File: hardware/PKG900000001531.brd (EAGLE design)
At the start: 80 x 50 mm, 297 parts, among them IC1 CAT24C256YI-G, IC2 FT232RQ, IC3 TPS62111, IC5 FT232RQ, IC6 SN74LVC1G126DCKR, IC7 SN74LVC1G126DCKR, J1 JST-GH-5H, J10 FPC-15VERT, J11 FPC-15VERT, J12 JST-GH-6H, J13 JST-GH-6H, J14 JST-GH-4H, J2 DF40HC(3.0)-100DS-0.4V(51), J3 USD_WURTH, J4 DIP-1, J5 SM10B-SRSS-TB, J7 USB-TYPE-C, J8 DF40HC(3.0)-100DS-0.4V(51), J9 CON8X3STD, Q1 FDN360P, Q2 DNP, Q3 FDN360P, Q4 FDN360P, Q6 FDN360P, U1 TPS2041BDGN, U10 DNP, U100 STM32H753II, U101 MIC94081, U102 USB2513, U105 TPS2121, U106 FM25V02A-DG, U107 TPD4E02B0410-USON, U108 BMP388, U109 MIC94081, U11 ICM-20602, U110 TCR2EF18, U13 USB3300-EZK-TR, U15 BMI088, U16 MIC94081, U17 TPD4E02B0410-USON, U18 TPD4E02B0410-USON, U2 TJA1051TK/3, U25 TPS2041BDGN, U26 TS3USB30, U3 TPD4E02B0410-USON, U4 EVQ, U5 G313-06329-00, U6 NCP308, U7 ICM-42605, U8 TPD4E02B0410-USON, U9 BMM150, Y1 24.000MHz, Y2 16.000MHz, Y3 32.768KHz CL6, Y4 24.000MHz

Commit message: Update hardware files for revision 2.
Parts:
- removed U$57: DNP, qualified_1:GEPPETTO_HOLE_2.9
- added R13, R47, R55, R56: 10K 1%, qualified_1:0201
- added R46: DNP, qualified_1:0201
- added R52, R54: 0R, qualified_1:0201
- added U30: TS3A5223, qualified_1:UQFN-10
- R77: value DNP -> 10K 1%
- moved C68 3.06 mm to (36.1, 10.5), turned to 270 degrees
- renumbered U4 to S3
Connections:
- removed net 3V3_SPEKTRUM$1: U16.1_1, U16.1_2
- removed net 5.USB_DEVICE_VBUS: FB4.1
- removed net 6.USB_DEVICE_VBUS: FB1.1
- new net 3V3_SPEKTRUM: J1.P4, U16.1_1, U16.1_2
- new net BMM150_PS: R46.2, R47.1, U9.A1
- new net UART_MUX_SEL$: R55.1, R56.2, U30.4, U30.8
- new net USART3_RX_DEBUG_FTDI: IC6.4, U30.2
- new net USART3_RX_DEBUG_JST: D5.A, U30.5
- new net USART3_TX_DEBUG_FTDI: IC5.2, U30.10
- new net USART3_TX_DEBUG_JST: J5.2, U3.1, U3.10, U30.7
- net 2.3.3V_VCC_3.3: now also U30.1; no longer J1.P4
- net 3V3_SENSORS: now also R47.2
- net 7.UART4_4W_RXD: now also R54.1
- net 7.UART4_4W_TXD: now also R52.1
- net BTN_A$22: now also S1.B@1
- net GND: now also R13.1, R46.1, R56.1, S1.A@2, U30.6; no longer U9.A1
- net SDO$1: now also R13.2
- net UART5_CTS_TELEM2: now also R1.2, R2.2
- net UART5_RTS_TELEM2: now also R3.2, R4.2
- net UART5_RX_TELEM2: now also R52.2
- net UART5_TX_TELEM2: now also R54.2
- net UART7_CTS_TELEM1: no longer R1.2, R2.2
- net UART7_RTS_TELEM1: no longer R3.2, R4.2
- net USART3_RX_DEBUG: now also U30.3; no longer D5.A, IC6.4
- net USART3_TX_DEBUG: now also U30.9; no longer IC5.2, J5.2, U3.1, U3.10
- net VBUS_SENSE: now also FB1.1, FB4.1, R55.2
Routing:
- net USART3_TX_DEBUG_JST: track 0.00 -> 84.3 mm, vias 0 -> 4
- net USART3_RX_DEBUG_JST: track 0.00 -> 64.5 mm, vias 0 -> 2
- net 3V3_SPEKTRUM: track 0.00 -> 59.9 mm, vias 0 -> 1
- net USART3_TX_DEBUG: track 93.0 -> 44.8 mm, vias 4 -> 2
- net UART5_CTS_TELEM2: track 0.00 -> 44.4 mm, vias 0 -> 3
- net UART5_RTS_TELEM2: track 0.00 -> 41.6 mm, vias 0 -> 3
- net 7.UART4_4W_RXD: track 0.00 -> 39.6 mm, vias 0 -> 3
- net 7.UART4_4W_TXD: track 0.00 -> 37.8 mm, vias 0 -> 3
- net VBUS_SENSE: track 43.0 -> 66.7 mm
- net USART3_RX_DEBUG: track 105.8 -> 84.9 mm, vias 3 -> 2
- net UART7_RTS_TELEM1: track 20.9 -> 0.00 mm, vias 2 -> 0
- net USART3_TX_DEBUG_FTDI: track 0.00 -> 16.8 mm
- net USART3_RX_DEBUG_FTDI: track 0.00 -> 12.6 mm, vias 0 -> 1
- net UART7_CTS_TELEM1: track 12.4 -> 0.00 mm, vias 2 -> 0
- net UART5_TX_TELEM2: track 0.00 -> 10.4 mm, vias 0 -> 1
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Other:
- board text added: "DFU"
- board text added: "OTG HS"

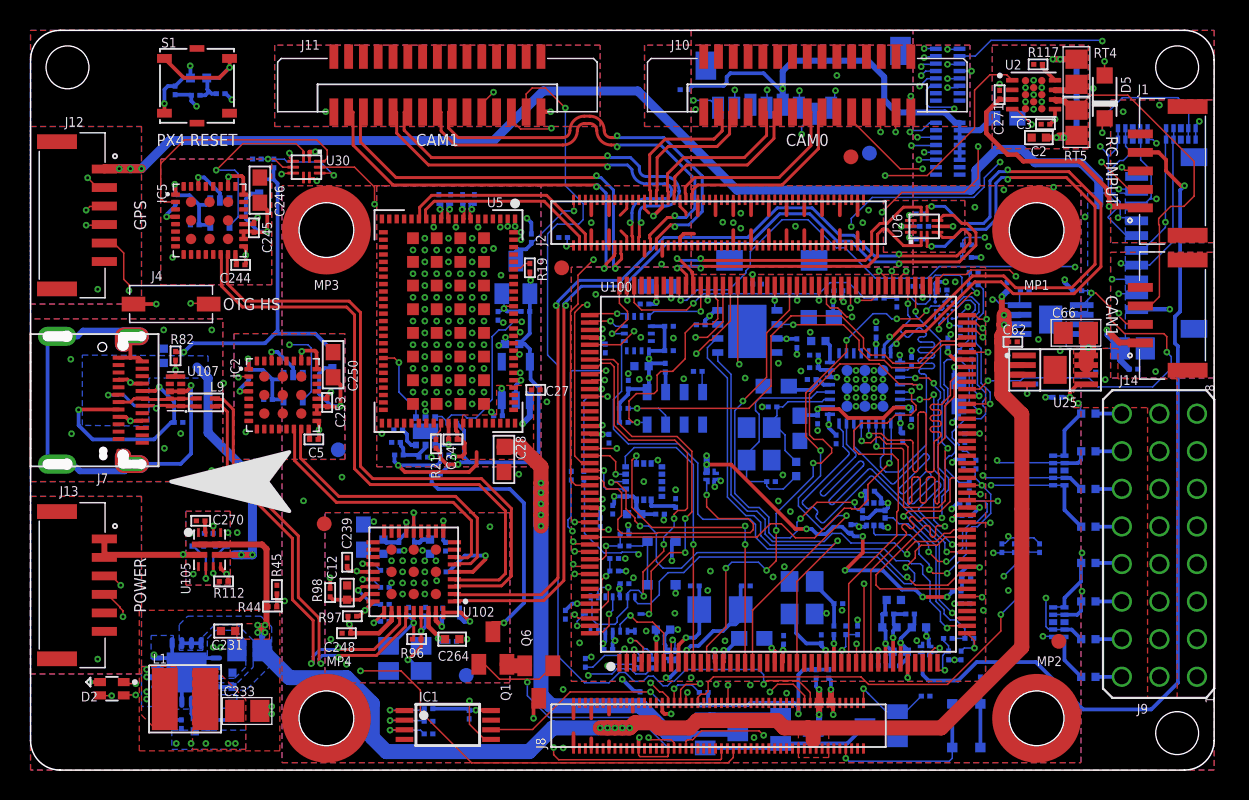
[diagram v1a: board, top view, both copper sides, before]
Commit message: Update board design files to v4.
Add ROS2 and Coral support information to the firmware docs.
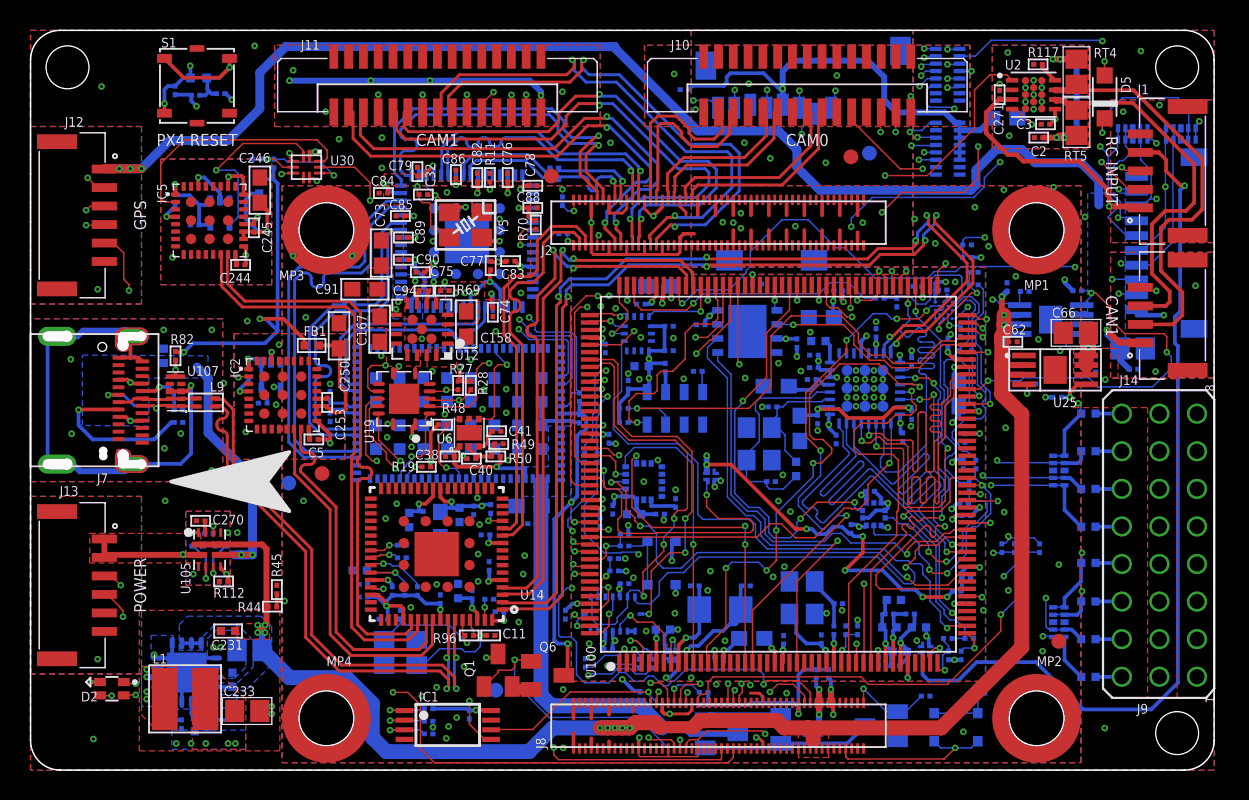
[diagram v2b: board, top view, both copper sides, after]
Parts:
- removed C103: 0.1uF, qualified_1@eagle_src_repo_a6c39d613d14f2251c563284af21e76ddd4db3e9:0201
- removed C242, C272, C273: 0.1uF, qualified_1:0201
- removed C264: 1.0uF, qualified_1:0402
- removed J4: DIP-1, qualified_1:CHS-01TA
- removed Q2: DNP, qualified_1:SOT23
- removed R116: DNP, qualified_1:0201
- removed R118, R121, R122: 0R, qualified_1:0201
- removed U102: USB2513, qualified_1:QFN36-6X6MM
- removed U110: TCR2EF18, qualified_1:SOT-23-5
- removed U26: TS3USB30, qualified_1:UQFN-10
- added C158, C167: 10uF, qualified_1:0603
- added C31, C96: 1.0uF, qualified_1:0402
- added C32: 10pF, qualified_1:0201
- added C72, C73, C74, C75, C76, C77, C78, C79, C82, C83, C84, C85, C86, C88, C89, C92, C93, C95, C97: 0.1uF, qualified_1:0201
- added C90, C91: 4.7uF / 16V, qualified_1:0603
- added C94: 6.8nF, qualified_1:0201
- added R58: 0R, qualified_1:0201
- added R68: 5K1, qualified_1:0201
- added R69, R70: 10K 1%, qualified_1:0201
- added U12: ADP1740ACPZ-1.2-R7, qualified_1:LFCSPWQ16
- added U14: USB2517-JZX, qualified_1:QFN64-9X9MM-FT2232HQ
- added U19: (no value), qualified_1:S-PVQFN-N14
- added U4: ASM1142, qualified_1:QFN64-9X9MM-FT2232HQ
- added Y5: 20.000MHz, qualified_1:CRYSTAL-3225
- C13, C16: value 1.0uF -> 0.1uF; device qualified_1:0402 -> qualified_1:0201
- C2: value DNP -> 4.7nF; device qualified_1:0402 -> qualified_1:0201
- R11: value 10K 1% -> 12K1
- R117: value DNP -> 10K 1%
- R20: value DNP -> 1K5
- R27, R28: value 10K 1% -> 1K5; device qualified_1@eagle_src_repo_a6c39d613d14f2251c563284af21e76ddd4db3e9:0201 -> qualified_1:0201
- R43, R9: value DNP -> 0R
- R5: value 0R -> 100K 1%
- RT4, RT5: value DNP -> 60R4
- U$2: device qualified_1:GEPPETTO_LABEL_SMALL -> qualified_1:UPVERTER_LABEL_SMALL
- U6: value NCP308 -> (none)
- moved R11 47.5 mm to (31.1, 40.0), flipped to the top
- moved R20 41.4 mm to (64.5, 5.50), turned to 270 degrees
- moved R27 32.8 mm to (28.9, 26.0), flipped to the top, turned to 90 degrees
- moved R28 32.5 mm to (29.8, 26.0), flipped to the top, turned to 90 degrees
- moved R5 21.0 mm to (31.1, 17.6)
- moved R19 15.2 mm to (26.8, 20.5), turned to 0 degrees
- moved C16 11.4 mm to (21.6, 31.6), turned to 180 degrees
- moved R21 10.2 mm to (37.1, 25.2), flipped to the bottom
- moved C27 9.05 mm to (33.9, 16.6), flipped to the bottom
- moved C34 8.66 mm to (37.1, 23.8), flipped to the bottom, turned to 270 degrees
- moved R43 8.12 mm to (20.2, 23.9), turned to 90 degrees
- moved R49 6.95 mm to (31.6, 22.1), flipped to the top
- moved C41 6.65 mm to (31.5, 22.9), flipped to the top
- moved R50 6.55 mm to (31.4, 21.2), flipped to the top
- moved U5 6.29 mm to (28.9, 24.1), flipped to the bottom, turned to 180 degrees
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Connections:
- removed net !PCIE_CLKREQ$17: Q2.2, R116.2, R20.2, U5.78
- removed net 1.USB_HS_VBUS: U13.4
- removed net 1.USB_MUX_D_N: U102.1, U26.5
- removed net 1.USB_MUX_D_P: U102.2, U26.3
- removed net 7.PCIE_CLK_N: R121.2, U5.10
- removed net 7.PCIE_CLK_P: R118.2, U5.11
- removed net CC$3: J7.A5, J7.B5, R89.2
- removed net INTR$17: U5.77
- removed net PCIE_TX_N$17: U5.4
- removed net PCIE_TX_P$17: U5.5
- removed net RPIBOOT_SWITCH$7: R11.2, S2.1, S2.2
- removed net SELECT: J4.2, R27.2, U26.10
- removed net USBMUX_OE$13: R28.2, U26.8
- removed net USB_CRFILT$4: C13.1, C272.1, U102.14
- removed net USB_PLLFILT$4: C242.1, C264.1, U102.34
- removed net USB_VBUS_DET$4: R97.2, U102.27
- removed net V1.8$17: C16.1, Q2.1, R116.1, R19.2, R21.2, R43.2, R48.2, U110.5
- new net !INT: U4.2
- new net !PCIE_WAKE: U4.25
- new net !RST$: R70.1, U4.9
- new net !SPI_CS$: U4.7
- new net !USB1_NOC: U4.28
- new net !USB2_NOC: U4.29
- new net 7.GPIO2_GPIO: J8.58, U19.11
- new net 7.GPIO3_GPIO: J8.56, U19.10
- new net 7.GPIO6_GPIO: J8.30, U19.12
- new net 7.GPIO7_GPIO: J8.37, U19.13
- new net 7.PCIE_NRESET: J2.9, R69.1, U4.30
- new net CC1$3: J7.A5, R68.2
- new net CC2$3: J7.B5, R89.2
- new net CFG_SEL2$: R5.2, U14.13
- new net I2C_SCL: R27.1, U19.5, U5.50
- new net I2C_SDA: R28.1, U19.4, U5.49
- new net PCIE_CLK_N: J2.12, U4.49
- new net PCIE_CLK_P: J2.10, U4.48
- new net PCIE_RX0__N: C93.2, U4.57
- new net PCIE_RX0__P: C92.2, U4.56
- new net PCIE_TX_N: J2.24, U4.53
- new net PCIE_TX_P: J2.22, U4.54
- new net PHY_PRG: U19.2, U5.84
- new net REXT$: R11.2, U4.59
- new net RPIBOOT_SWITCH$19: R20.2, S2.1, S2.2
- new net SPI_CLK$: U4.5
- new net SPI_DI$: U4.8
- new net SPI_DO$: U4.6
- new net UART_RX$: U4.10
- new net UART_TX$: U4.11
- new net USB1_N: U4.22, U5.14
- new net USB1_P: U4.23, U5.13
- new net USB1_PWREN: U4.26
- new net USB1_SSRX_N: U4.46, U5.4
- new net USB1_SSRX_P: U4.45, U5.5
- new net USB1_SSTX_N: C16.2, U4.43
- new net USB1_SSTX_P: C72.2, U4.42
- new net USB1_SSTX__N: C16.1, U5.7
- new net USB1_SSTX__P: C72.1, U5.8
- new net USB2_N: U4.18
- new net USB2_P: U4.19
- new net USB2_PWREN: U4.27
- new net USB2_SSRX_N: U4.37
- new net USB2_SSRX_P: U4.36
- new net USB2_SSTX_N: U4.40
- new net USB2_SSTX_P: U4.39
- new net USB_CRFILT$: C31.1, C95.1, U14.25
- new net USB_PLLFILT$: C96.1, C97.1, U14.62
- new net V1.2$: C167.1, C74.1, C75.1, C78.1, C79.1, C82.1, C83.1, C84.1, C89.1, C90.1, C91.1, U12.10, U12.11, U12.12, U12.13, U12.14, U12.9, U4.1, U4.12, U4.21, U4.33, U4.34, U4.35, U4.41, U4.47, U4.52, U4.58
- new net VBUS_DET$: R97.2, U14.44
- new net VCC1V1_SS$: C94.1, U12.7
- new net XI$: C32.2, U4.51, Y5.1
- new net XO$: C32.1, U4.50, Y5.3
- new net _PCIE_CLK_N: R43.2, U5.10
- new net _PCIE_CLK_P: R58.2, U5.11
- net 1.USB_HS_D_N: now also U14.1; no longer U26.6
- net 1.USB_HS_D_P: now also U14.2; no longer U26.2
- net 2.3.3V_VCC_3.3: now also C13.1, C158.1, C73.1, C76.1, C77.1, C85.1, C86.1, C88.1, R5.1, R69.2, R70.2, R91.1, U12.1, U12.15, U12.16, U12.2, U12.3, U12.4, U14.10, U14.24, U14.46, U14.5, U14.52, U14.57, U14.64, U4.20, U4.24, U4.32, U4.38, U4.4, U4.44, U4.55, U4.62; no longer C103.1, J4.1, U102.10, U102.15, U102.23, U102.29, U102.36, U102.5, U26.9
- net 4.USB_D_N: now also U14.58; no longer U102.30
- net 4.USB_D_P: now also U14.59; no longer U102.31
- net 5.USB_DEVICE_D_N: now also U14.53; no longer U102.3
- net 5.USB_DEVICE_D_P: now also U14.54; no longer U102.4
- net 6.USB_DEVICE_D_N: now also U14.55; no longer U102.6
- net 6.USB_DEVICE_D_P: now also U14.56; no longer U102.7
- net 7.1.8V_VCC_1.8: now also C34.1, R19.2, R21.2, R27.2, R28.2, R48.2, U19.1, U19.8, U5.54; no longer R43.1
- net 7.3.3V_VCC_3.3: now also U19.14; no longer C273.1, C34.1, R9.1, U110.1, U110.3, U5.54
- net 7.PCIE_CLKREQ_GPIO: now also R9.1; no longer Q2.3, R9.2
- net CORAL_D_N: now also J2.3, U14.11; no longer J2.5, U5.14
- net CORAL_D_P: now also J2.5, U14.12; no longer J2.3, U5.13
- net GND: now also C158.2, C167.2, C31.2, C73.2, C74.2, C75.2, C76.2, C77.2, C78.2, C79.2, C82.2, C83.2, C84.2, C85.2, C86.2, C88.2, C89.2, C90.2, C91.2, C94.2, C95.2, C96.2, C97.2, R43.1, R58.1, R68.1, R9.2, U12.6, U12.EP, U12.EP1, U12.EP2, U12.EP3, U12.EP4, U14.19, U14.65, U14.EPAD1, U14.EPAD10, U14.EPAD11, U14.EPAD12, U14.EPAD2, U14.EPAD3, U14.EPAD4, U14.EPAD5, U14.EPAD6, U14.EPAD7, U14.EPAD8, U14.EPAD9, U19.7, U4.15, U4.65, U4.EPAD1, U4.EPAD10, U4.EPAD11, U4.EPAD12, U4.EPAD2, U4.EPAD3, U4.EPAD4, U4.EPAD5, U4.EPAD6, U4.EPAD7, U4.EPAD8, U4.EPAD9, Y5.2, Y5.4; no longer C103.2, C16.2, C242.2, C264.2, C272.2, C273.2, R118.1, R121.1, R122.1, R27.1, R28.1, R5.1, R91.1, U102.EPAD, U102.EXP1, U102.EXP2, U102.EXP3, U102.EXP4, U102.EXP5, U102.EXP6, U102.EXP7, U102.EXP8, U110.2, U26.4
- net PCIE_RX_N: now also C92.1, J2.18; no longer R5.2, U5.8
- net PCIE_RX_P: now also C93.1, J2.16; no longer R122.2, U5.7
- net PMIC_EN$17: now also U19.3
- net USB_D_N: now also U14.3; no longer U26.7
- net USB_D_P: now also U14.4; no longer U26.1
- net USB_HS_IND$4: now also U14.42; no longer U102.25
- net USB_NRESET$4: now also U14.43; no longer U102.26
- net USB_RBIAS$4: now also U14.63; no longer U102.35
- net USB_SCL$4: now also U14.41; no longer U102.24
- net USB_SDA$4: now also U14.40; no longer U102.22
- net USB_SUSP_IND$4: now also U14.45; no longer U102.28
- net USB_XTAL1$4: now also U14.61; no longer U102.33
- net USB_XTAL2$4: now also U14.60; no longer U102.32
- net VBUS_SENSE: now also U13.4
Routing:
- net 1.USB_MUX_D_N: track 63.5 -> 0.00 mm, vias 2 -> 0
- net SELECT: track 63.3 -> 0.00 mm, vias 3 -> 0
- net 1.USB_MUX_D_P: track 62.2 -> 0.00 mm, vias 2 -> 0
- net 7.GPIO3_GPIO: track 0.00 -> 56.6 mm, vias 0 -> 3
- net 7.GPIO2_GPIO: track 0.00 -> 52.8 mm, vias 0 -> 3
- net 7.GPIO6_GPIO: track 0.00 -> 45.8 mm, vias 0 -> 3
- net 7.GPIO7_GPIO: track 0.00 -> 43.2 mm, vias 0 -> 3
- net 1.SD_CARD_POWER: track 93.5 -> 131.4 mm
- net 7.1.8V_VCC_1.8: track 17.4 -> 51.6 mm, vias 1 -> 6
- net 2.3.3V_VCC_3.3: track 87.7 -> 121.1 mm, vias 57 -> 66
- net 1.USB_HS_D_P: track 38.4 -> 67.1 mm, vias 3 -> 5
- net 1.USB_HS_D_N: track 39.1 -> 67.8 mm, vias 3 -> 5
- net USB1_SSRX_N: track 0.00 -> 27.5 mm
- net USB1_SSRX_P: track 0.00 -> 27.3 mm
- net V1.8$17: track 25.7 -> 0.00 mm, vias 2 -> 0
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- added copper zone on layer 1, net 13.VCC_VCC_5.0
- added copper zone on layer 16, net 7.3.3V_VCC_3.3
- added copper zone on layer 1, net V1.2$
- added copper zone on layer 16, net V1.2$
- removed copper zone on layer 1, net 7.3.3V_VCC_3.3
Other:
- board text removed: "OTG HS"
